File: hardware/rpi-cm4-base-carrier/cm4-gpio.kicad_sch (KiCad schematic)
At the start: 10 parts, among them J2 DNP, J3 USB4105-GF-A, J4 SM04B-SRSS-TB(LF)(SN)

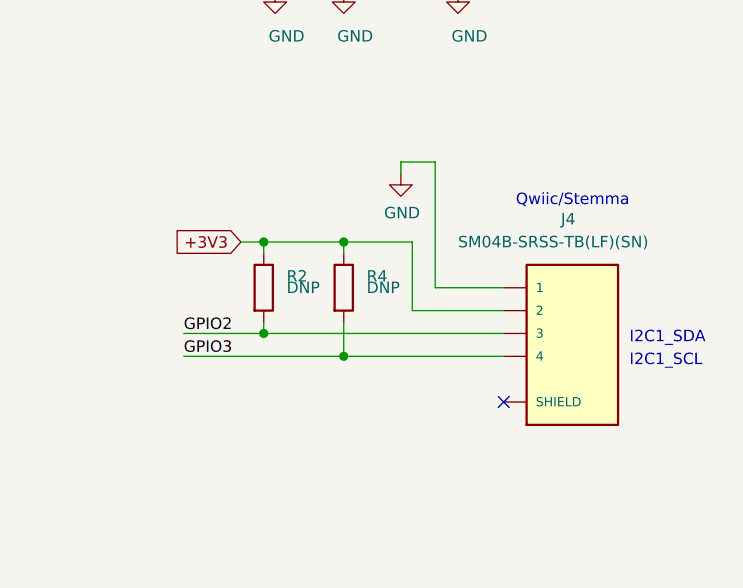
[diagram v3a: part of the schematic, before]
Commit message: started to route core connectors to CM4, RJ45 annoyingly has the inverse pinout to CM4, need to work out how to uncross tracking sensibly
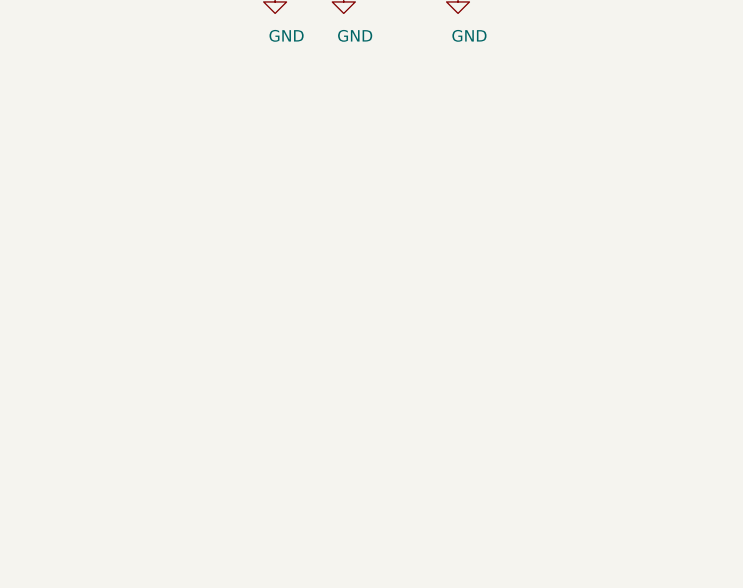
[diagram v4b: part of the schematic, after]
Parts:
- removed J4: SM04B-SRSS-TB(LF)(SN), SM04B-SRSS-TB_LF__SN_:JST_SM04B-SRSS-TB(LF)(SN), symbol SM04B-SRSS-TB_LF__SN_:SM04B-SRSS-TB(LF)(SN)
- removed R2, R4: DNP, Resistor_SMD:R_0603_1608Metric_Pad0.98x0.95mm_HandSolder, symbol Device:R
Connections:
- no-connect marks 7 -> 6
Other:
- note removed: "I2C1_SCL"
- note removed: "I2C1_SDA"
- note removed: "Qwiic/Stemma"

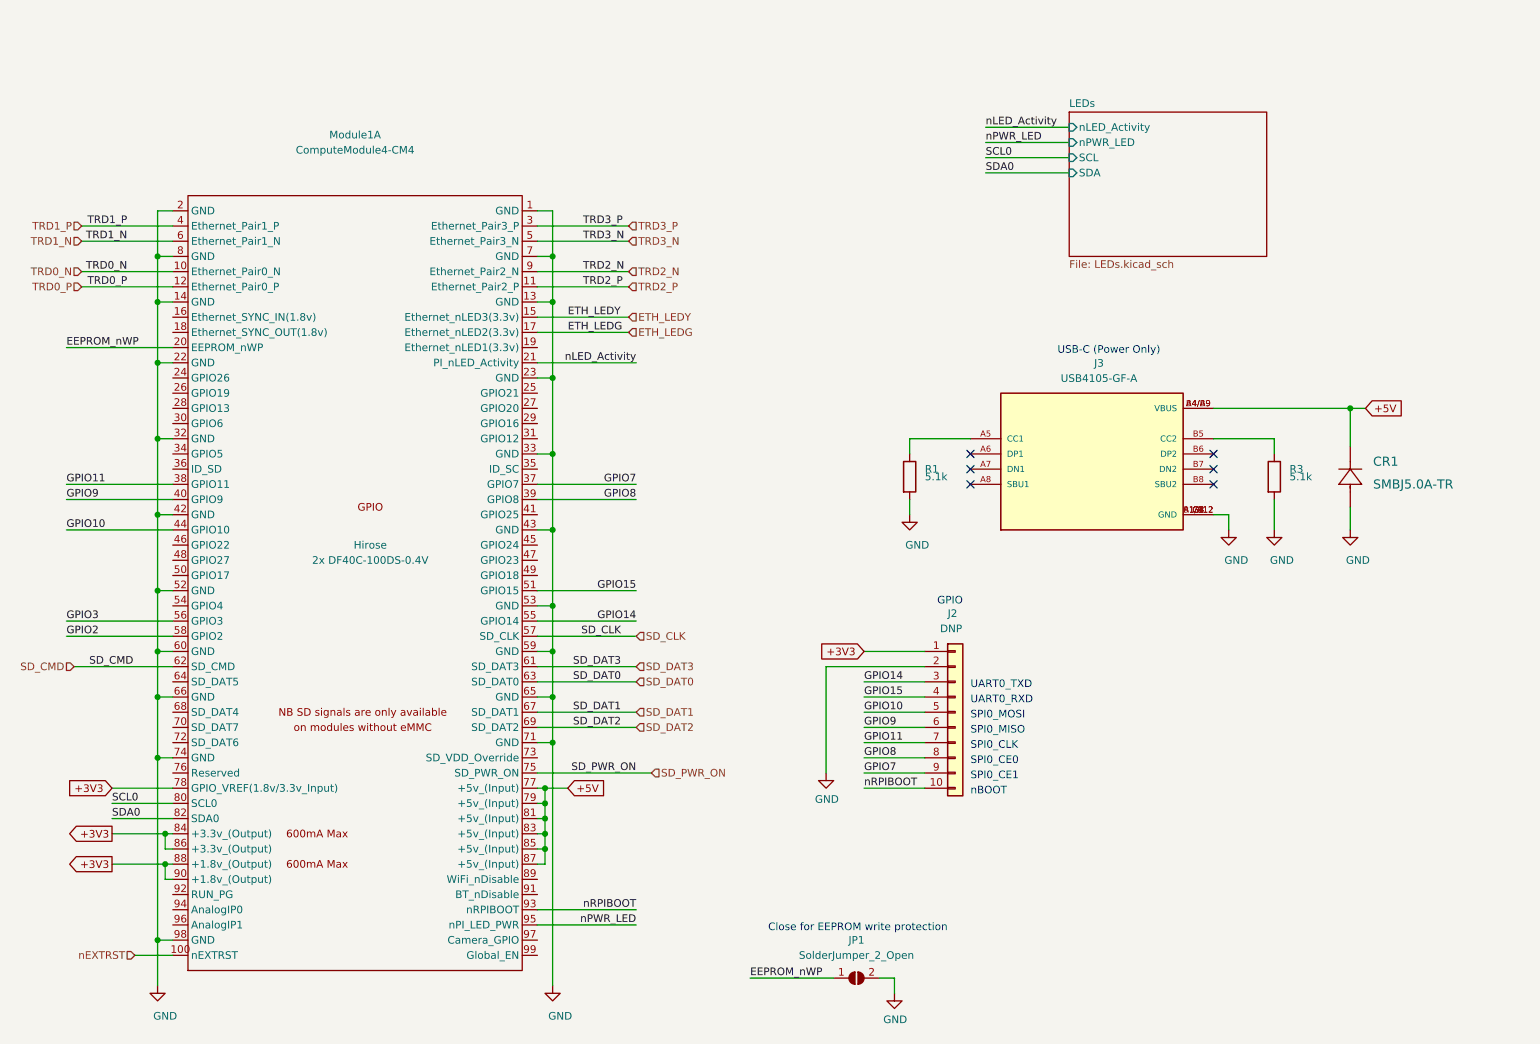
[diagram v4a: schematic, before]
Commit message: schematic entry for samtec board edge connector complete, started breakout of GPIO lines for connection to board edge connector
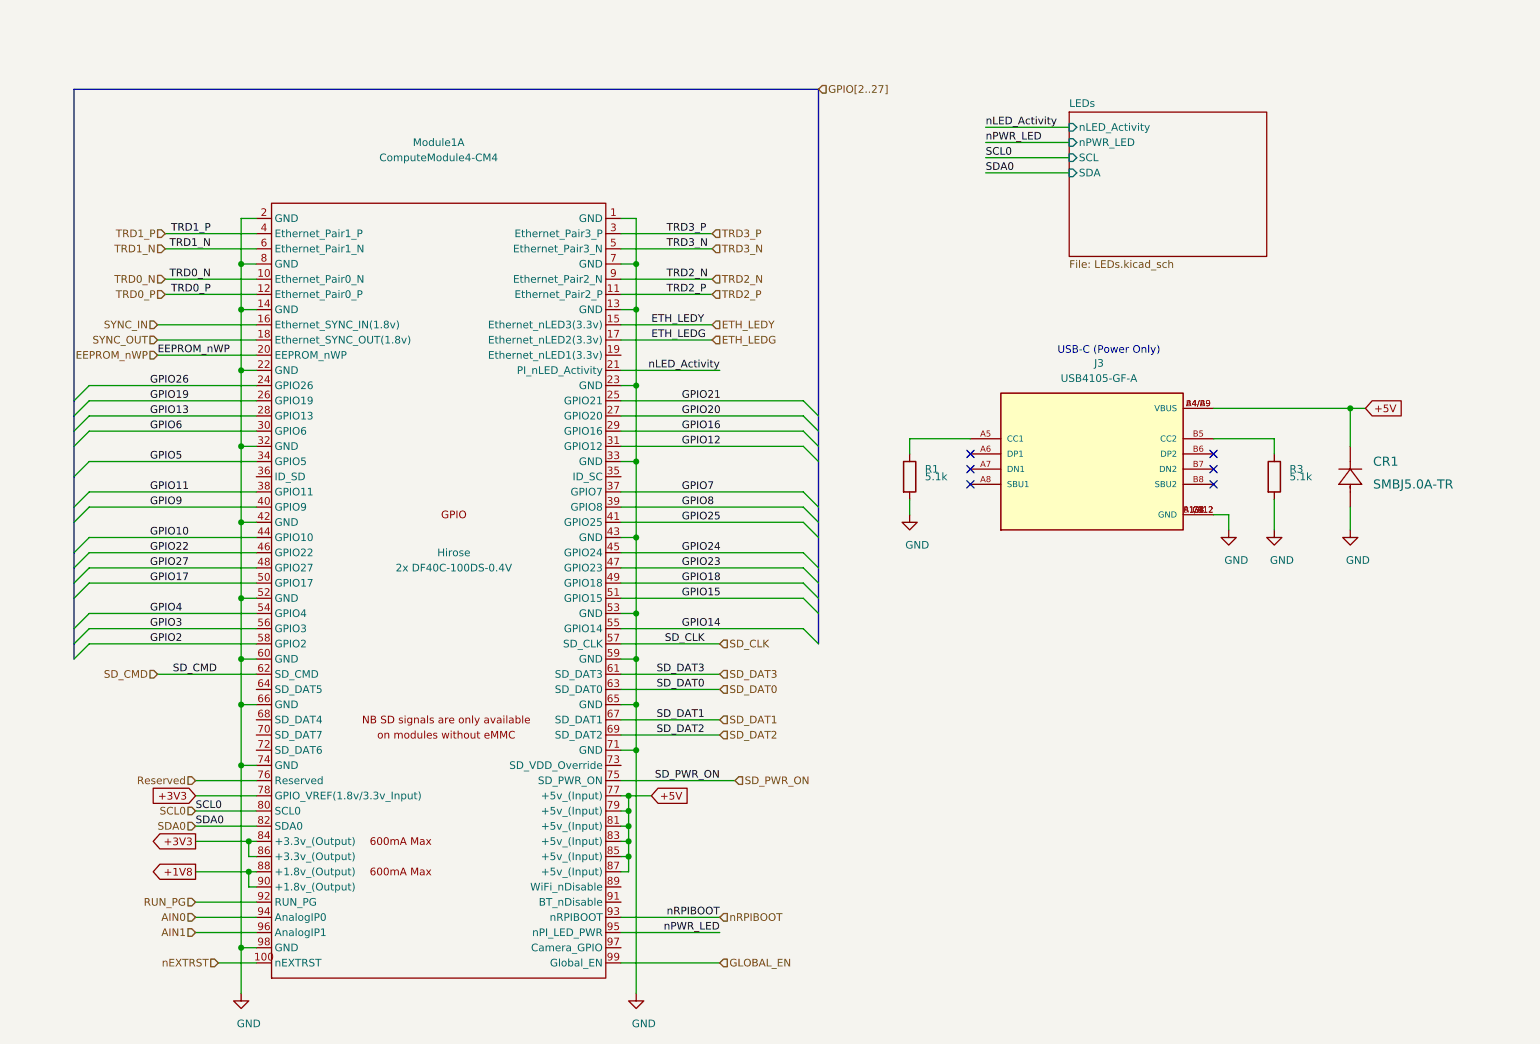
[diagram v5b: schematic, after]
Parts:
- removed J2: DNP, Connector_PinHeader_2.54mm:PinHeader_1x10_P2.54mm_Vertical, symbol Connector_Generic:Conn_01x10
- removed JP1: SolderJumper_2_Open, Jumper:SolderJumper-2_P1.3mm_Open_RoundedPad1.0x1.5mm, symbol Jumper:SolderJumper_2_Open
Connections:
- net +3V3: no longer Module1.88 (+1.8v_(Output)), Module1.90 (+1.8v_(Output))
- net SYNC_IN: now reaches Module1.16 (Ethernet_SYNC_IN(1.8v))
- net SYNC_OUT: now reaches Module1.18 (Ethernet_SYNC_OUT(1.8v))
- net GPIO26: now reaches Module1.24 (GPIO26)
- net GPIO21: now reaches Module1.25 (GPIO21)
- net GPIO19: now reaches Module1.26 (GPIO19)
- net GPIO20: now reaches Module1.27 (GPIO20)
- net GPIO13: now reaches Module1.28 (GPIO13)
- net GPIO16: now reaches Module1.29 (GPIO16)
- net GPIO6: now reaches Module1.30 (GPIO6)
- net GPIO12: now reaches Module1.31 (GPIO12)
- net GPIO5: now reaches Module1.34 (GPIO5)
- net GPIO25: now reaches Module1.41 (GPIO25)
- net GPIO24: now reaches Module1.45 (GPIO24)
- net GPIO22: now reaches Module1.46 (GPIO22)
- net GPIO23: now reaches Module1.47 (GPIO23)
- net GPIO27: now reaches Module1.48 (GPIO27)
- net GPIO18: now reaches Module1.49 (GPIO18)
- net GPIO17: now reaches Module1.50 (GPIO17)
- net GPIO4: now reaches Module1.54 (GPIO4)
- net Reserved: now reaches Module1.76 (Reserved)
- net RUN_PG: now reaches Module1.92 (RUN_PG)
- net AIN0: now reaches Module1.94 (AnalogIP0)
- net AIN1: now reaches Module1.96 (AnalogIP1)
- net GLOBAL_EN: now reaches Module1.99 (Global_EN)
- new net +1V8: Module1.88 (+1.8v_(Output)), Module1.90 (+1.8v_(Output))
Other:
- note removed: "Close for EEPROM write protection"
- note removed: "GPIO"
- note removed: "SPI0_CE0"
- note removed: "SPI0_CE1"
- note removed: "SPI0_CLK"
- note removed: "SPI0_MISO"
- note removed: "SPI0_MOSI"
- note removed: "UART0_RXD"
- note removed: "UART0_TXD"
- note removed: "nBOOT"
- moved on the sheet: Module1A

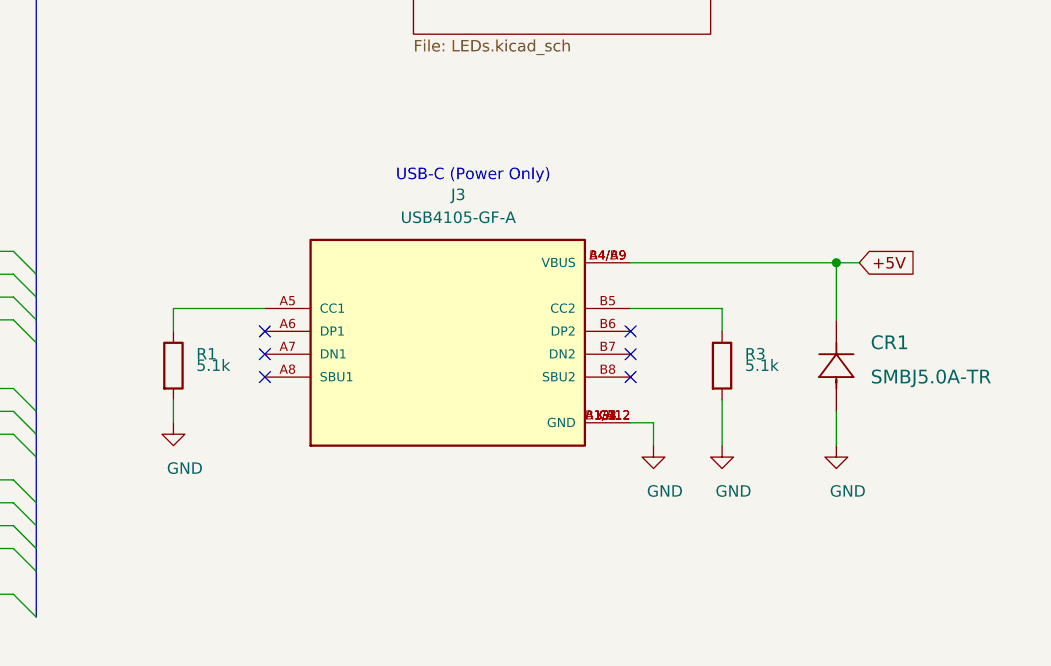
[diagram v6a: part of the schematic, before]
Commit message: redundant USBC power schematic created, layout of single USBC input completed@
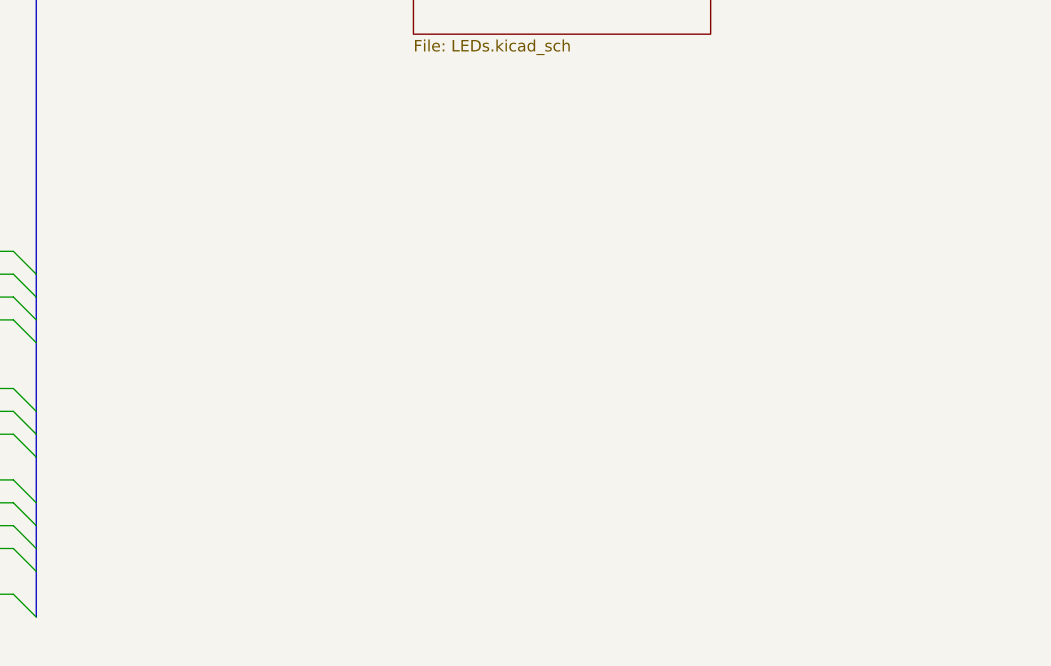
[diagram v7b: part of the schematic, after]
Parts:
- removed CR1: SMBJ5.0A-TR, footprints:SMBJ5.0A-TR, symbol 2020-11-06_22-01-36:SMBJ5.0A-TR
- removed J3: USB4105-GF-A, USB4105-GF-A:GCT_USB4105-GF-A, symbol USB4105-GF-A:USB4105-GF-A
- removed R1, R3: 5.1k, Resistor_SMD:R_0603_1608Metric_Pad0.98x0.95mm_HandSolder, symbol Device:R
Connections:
- no-connect marks 6 -> 0
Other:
- note removed: "USB-C (Power Only)"

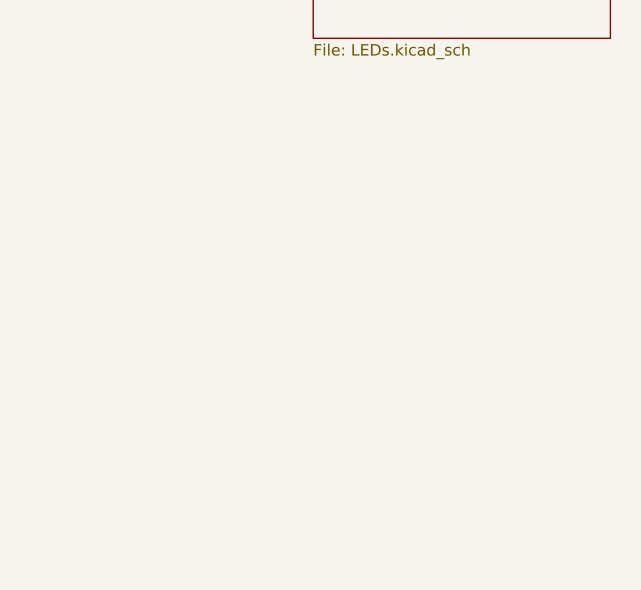
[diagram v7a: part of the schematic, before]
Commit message: fan control added to sch, layout 90% complete, awaiting review
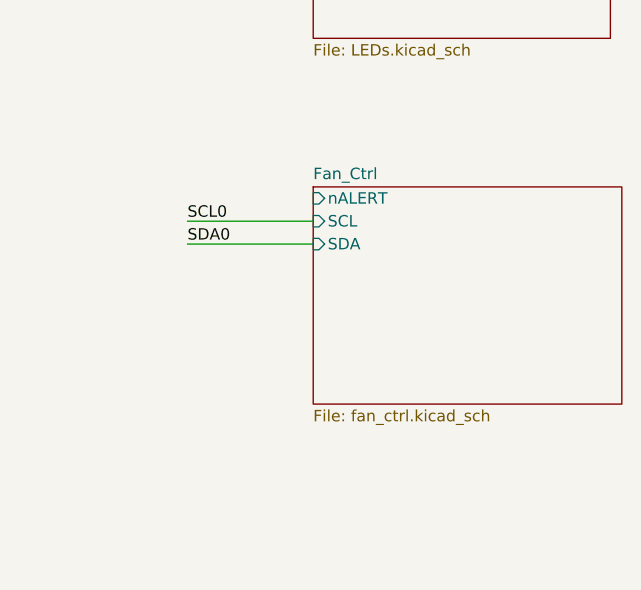
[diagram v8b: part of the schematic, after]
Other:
- added sheet Fan_Ctrl (fan_ctrl.kicad_sch)
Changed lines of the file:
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@@
     (stroke (width 0) (type solid))
+  )
+  (wire (pts (xy 179.07 76.2) (xy 193.04 76.2))
+    (stroke (width 0) (type default))
   )
   (wire (pts (xy 54.61 85.09) (xy 57.15 85.09))
@@
     (stroke (width 0) (type default))
   )
+  (wire (pts (xy 179.07 73.66) (xy 193.04 73.66))
+    (stroke (width 0) (type default))
+  )
   (wire (pts (xy 179.07 34.29) (xy 193.04 34.29))
     (stroke (width 0) (type solid))
@@
     (effects (font (size 1.27 1.27)) (justify left bottom))
   )
+  (label "SDA0" (at 179.07 76.2 0) (fields_autoplaced)
+    (effects (font (size 1.27 1.27)) (justify left bottom))
+  )
   (label "SCL0" (at 46.99 146.05 0) (fields_autoplaced)
     (effects (font (size 1.27 1.27)) (justify left bottom))
@@
   )
   (label "GPIO9" (at 39.37 95.25 0) (fields_autoplaced)
+    (effects (font (size 1.27 1.27)) (justify left bottom))
+  )
+  (label "SCL0" (at 179.07 73.66 0) (fields_autoplaced)
     (effects (font (size 1.27 1.27)) (justify left bottom))
   )
@@
       )
     )
+  )
+  (sheet (at 193.04 69.85) (size 34.29 24.13) (fields_autoplaced)
+    (stroke (width 0.1524) (type solid))
+    (fill (color 0 0 0 0.0000))
+    (property "Sheetname" "Fan_Ctrl" (at 193.04 69.1384 0)
+      (effects (font (size 1.27 1.27)) (justify left bottom))
+    )
+    (property "Sheetfile" "fan_ctrl.kicad_sch" (at 193.04 94.5646 0)
+      (effects (font (size 1.27 1.27)) (justify left top))
+    )
+    (pin "nALERT" input (at 193.04 71.12 180)
+      (effects (font (size 1.27 1.27)) (justify left))
+    )
+    (pin "SCL" input (at 193.04 73.66 180)
+      (effects (font (size 1.27 1.27)) (justify left))
+    )
+    (pin "SDA" input (at 193.04 76.2 180)
+      (effects (font (size 1.27 1.27)) (justify left))
+    )
+    (instances
+      (project "rpi-cm4-base-carrier"
+        (path "/92c58705-ecb0-498b-b561-44a3f0daad57/fc4c71a5-1008-4ac4-98db-57c838c57d91" (page "14"))
+      )
+    )
